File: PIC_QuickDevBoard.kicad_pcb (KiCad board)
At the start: 2 copper layers, 61.7 x 63.5 mm, 33 parts, among them J1 PICKitConnector, J10 Conn_01x08_Pin, J2 PowerSource, J3 USB_B_Micro, J4 Conn_01x08_Pin, J9 Conn_01x08_Pin, SW1 SW_Push, U1 PIC24, U2 PIC16, U3 LD1117, Y1 Crystal

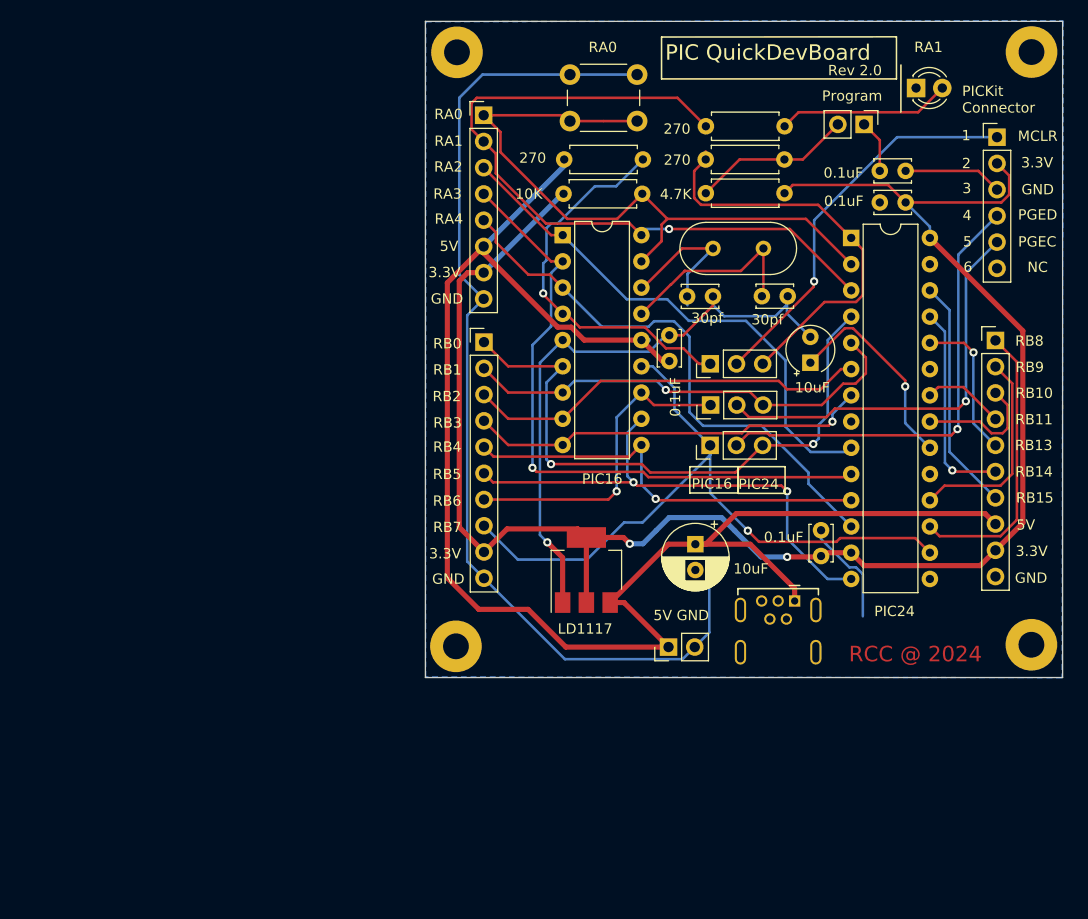
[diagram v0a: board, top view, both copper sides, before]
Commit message: fixing PICF14 vcc
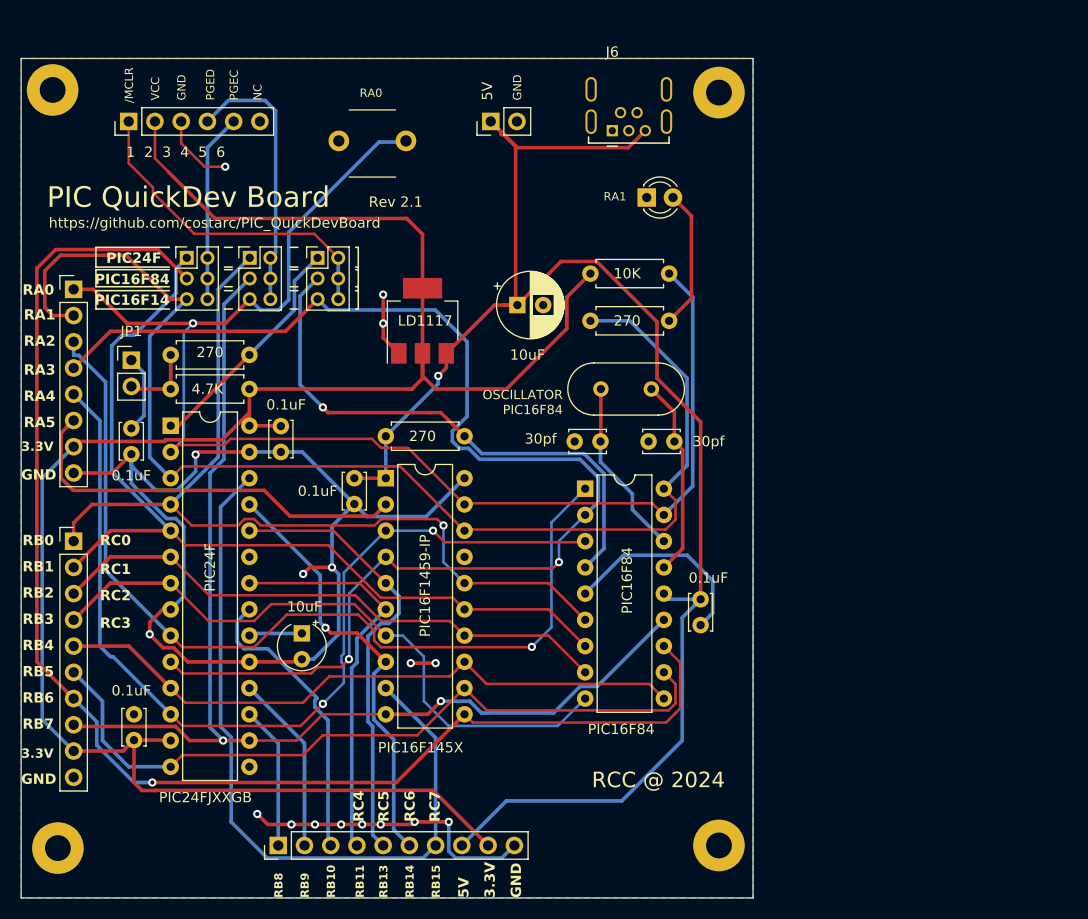
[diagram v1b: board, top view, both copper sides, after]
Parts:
- removed J10: Conn_01x08_Pin, Connector_PinHeader_2.54mm:PinHeader_1x10_P2.54mm_Vertical
- removed JP2: Jumper_MCLR, Connector_PinHeader_2.54mm:PinHeader_1x03_P2.54mm_Vertical
- removed JP3: Jumper_PGEC, Connector_PinHeader_2.54mm:PinHeader_1x03_P2.54mm_Vertical
- removed JP5: Program, Connector_PinHeader_2.54mm:PinHeader_1x02_P2.54mm_Vertical
- added C9: 0.1uF, Capacitor_THT:C_Disc_D3.4mm_W2.1mm_P2.50mm, F.Cu at (128.8, 85.4)
- added J5: PICKitConnector, Connector_PinHeader_2.54mm:PinHeader_1x06_P2.54mm_Vertical, F.Cu at (73.4, 39.1)
- added J6: USB_B_Micro, Roni_Footprints:USB_Mini-B_Tensility_4Holes, F.Cu at (120.2, 40.0)
- added J7: PGEC_LINES, Connector_PinHeader_2.00mm:PinHeader_2x03_P2.00mm_Vertical, F.Cu at (79.0, 52.3)
- added J8: PGED_LINES, Connector_PinHeader_2.00mm:PinHeader_2x03_P2.00mm_Vertical, F.Cu at (85.1, 52.3)
- added U4: PIC16F1459-IP, Package_DIP:DIP-20_W7.62mm, F.Cu at (98.3, 73.7)
- C4: value 0.1uF -> 10uF; footprint Capacitor_THT:C_Disc_D3.4mm_W2.1mm_P2.50mm -> Capacitor_THT:CP_Radial_Tantal_D4.5mm_P2.50mm
- C7: footprint Capacitor_THT:CP_Radial_Tantal_D4.5mm_P2.50mm -> Capacitor_THT:CP_Radial_D6.3mm_P2.50mm
- C8: value 10uF -> 0.1uF; footprint Capacitor_THT:CP_Radial_D6.3mm_P2.50mm -> Capacitor_THT:C_Disc_D3.4mm_W2.1mm_P2.50mm
- J1: value PICKitConnector -> Conn_01x08_Pin; footprint Connector_PinHeader_2.54mm:PinHeader_1x06_P2.54mm_Vertical -> Connector_PinHeader_2.54mm:PinHeader_1x08_P2.54mm_Vertical
- J2: value PowerSource -> Conn_01x08_Pin; footprint Connector_PinHeader_2.54mm:PinHeader_1x02_P2.54mm_Vertical -> Connector_PinHeader_2.54mm:PinHeader_1x10_P2.54mm_Vertical
- J3: value USB_B_Micro -> Conn_01x08_Pin; footprint Roni Footprints:USB_Mini-B_Tensility_4Holes -> Connector_PinHeader_2.54mm:PinHeader_1x10_P2.54mm_Vertical
- J4: value Conn_01x08_Pin -> PowerSource; footprint Connector_PinHeader_2.54mm:PinHeader_1x08_P2.54mm_Vertical -> Connector_PinHeader_2.54mm:PinHeader_1x02_P2.54mm_Vertical
- J9: value Conn_01x08_Pin -> MCLR_LINES; footprint Connector_PinHeader_2.54mm:PinHeader_1x10_P2.54mm_Vertical -> Connector_PinHeader_2.00mm:PinHeader_2x03_P2.00mm_Vertical
- JP1: value Jumper_PGED -> Program; footprint Connector_PinHeader_2.54mm:PinHeader_1x03_P2.54mm_Vertical -> Connector_PinHeader_2.54mm:PinHeader_1x02_P2.54mm_Vertical
- R3: value 10K -> 270
- R5: value 270 -> 10K
- SW1: footprint Button_Switch_THT:SW_PUSH_6mm -> Roni_Footprints:SW_PUSH_6mm_2Holes
- U1: value PIC24 -> PIC24F
- U2: value PIC16 -> PIC16F84
- moved C3 91.1 mm to (73.9, 99.0), turned to 90 degrees
- moved J1 90.6 mm to (68.1, 55.4)
- moved C1 76.6 mm to (73.7, 68.8), turned to -90 degrees
- moved U1 68.4 mm to (77.5, 68.6)
- moved J2 58.5 mm to (68.1, 79.8), turned to 0 degrees
- moved JP1 56.6 mm to (73.7, 62.2), turned to 0 degrees
- moved J3 55.3 mm to (87.9, 109.2), turned to 90 degrees
- moved R1 55.2 mm to (77.5, 65.0)
- moved C2 53.8 mm to (88.1, 68.6), turned to -90 degrees
- moved R2 48.1 mm to (85.1, 61.7), turned to 180 degrees
- moved C4 44.3 mm to (90.2, 88.7), turned to -90 degrees
- moved H3 43.2 mm to (66.5, 109.5)
- moved H1 39.3 mm to (66.0, 36.1)
- moved H4 36.0 mm to (130.6, 109.2)
- moved C8 33.6 mm to (95.2, 73.7)
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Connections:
- C1 pad 1: Net-(JP5-A) -> Net-(JP1-A)
- C4 pad 1: 5V -> Net-(U1-Vcap/Vddcore)
- C7 pad 1: Net-(U1-Vcap/Vddcore) -> 5V
- J1 pad 1: /MCLR -> PIC16F14_PGED
- J1 pad 2: 3.3V -> PIC16F14_PGEC
- J1 pad 3: GND -> RA2
- J1 pad 4: PGED -> PIC16F14_MCLR
- J1 pad 5: PGEC -> RA4
- J1 pad 6: unconnected-(J1-Pin_6-Pad6) -> RA5
- J2 pad 1: 5V -> PIC24_PGED
- J2 pad 2: GND -> PIC24_PGEC
- J3 pad 1: 5V -> RB8
- J3 pad 2: unconnected-(J3-D--Pad2) -> RB9
- J3 pad 3: unconnected-(J3-D+-Pad3) -> RB10
- J3 pad 4: unconnected-(J3-ID-Pad4) -> RB11
- J3 pad 5: GND -> RB13
- J3 pad 6: GND -> RB14
- J4 pad 1: RA0 -> 5V
- J4 pad 2: RA1 -> GND
- J9 pad 1: PIC24_PGED -> PIC24_MCLR
- J9 pad 2: PIC24_PGEC -> /MCLR
- J9 pad 3: RB2 -> PIC16F84_MCLR
- J9 pad 4: RB3 -> /MCLR
- J9 pad 5: RB4 -> PIC16F14_MCLR
- J9 pad 6: RB5 -> /MCLR
- JP1 pad 1: PIC16_PGED -> Net-(JP1-A)
- JP1 pad 2: PGED -> Net-(JP1-B)
- R1 pad 1: Net-(JP5-B) -> Net-(JP1-B)
- R2 pad 2: Net-(JP5-B) -> Net-(JP1-B)
- R3 pad 1: 3.3V -> PIC16F84_MCLR
- R3 pad 2: RA0 -> 5V
- R4 pad 1: RA1 -> PIC16F14_PGEC
- R5 pad 1: PIC16_MCLR -> 3.3V
- R5 pad 2: 5V -> PIC16F14_PGED
- SW1 pad 2: RA0 -> PIC16F14_PGED
- U1 pad 10: RA3 -> PIC16F14_MCLR
- U1 pad 16: PIC16_PGED -> PIC16F84_PGED
- U1 pad 2: RA0 -> PIC16F14_PGED
- U1 pad 3: RA1 -> PIC16F14_PGEC
- U2 pad 12: PIC16_PGEC -> PIC16F84_PGEC
- U2 pad 13: PIC16_PGED -> PIC16F84_PGED
- U2 pad 17: RA0 -> PIC16F14_PGED
- U2 pad 18: RA1 -> PIC16F14_PGEC
- U2 pad 2: RA3 -> PIC16F14_MCLR
- U2 pad 4: PIC16_MCLR -> PIC16F84_MCLR
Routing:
- net PIC16F14_PGED: track 0.00 -> 135.8 mm, vias 0 -> 1
- net PIC16F84_PGEC: track 0.00 -> 133.3 mm, vias 0 -> 1
- net PIC16F14_MCLR: track 0.00 -> 125.3 mm, vias 0 -> 2
- net PIC16F14_PGEC: track 0.00 -> 121.6 mm
- net PIC16F84_PGED: track 0.00 -> 110.4 mm, vias 0 -> 2
- net RA1: track 71.7 -> 0.00 mm, vias 1 -> 0
- net PIC16_PGED: track 68.0 -> 0.00 mm, vias 1 -> 0
- net RA0: track 65.0 -> 0.00 mm
- net RA3: track 63.0 -> 0.00 mm, vias 1 -> 0
- net PIC16F84_MCLR: track 0.00 -> 53.8 mm, vias 0 -> 1
- net RB15: track 22.7 -> 73.9 mm
- net PIC24_PGEC: track 44.2 -> 88.1 mm, vias 1 -> 0
- net RA5: track 0.00 -> 39.5 mm
- net PIC16_MCLR: track 38.0 -> 0.00 mm, vias 1 -> 0
- net RA2: track 50.9 -> 88.8 mm, vias 0 -> 1
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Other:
- board size 61.7 x 63.5 mm -> 70.9 x 81.3 mm
- board text added: "/MCLR"
- board text added: "1 2 3 4 5 6"
- board text added: "OSCILLATOR PIC16F84"
- board text added: "PIC QuickDev Board"
- board text added: "PIC16F14"
- board text added: "PIC16F145X"
- board text added: "PIC16F84"
- board text added: "PIC24F"
- board text added: "PIC24FJXXGB"
- board text added: "RA5"
- board text added: "RC0"
- board text added: "RC1"
- board text added: "RC2"
- board text added: "RC3"
- board text added: "RC4"
- board text added: "RC5"
- board text added: "RC6"
- board text added: "RC7"
- board text added: "Rev 2.1"
- board text added: "VCC"
- board text removed: "1"
- board text removed: "2"
- board text removed: "3"
- board text removed: "4"
- board text removed: "5"
- board text removed: "5V GND"
- board text removed: "6"
- board text removed: "For PIC16 use: Insert the 3 jumpers in position {dblquote}PIC16{dblquote} For PIC24 use: Insert the 3 jumpers in position {dblquote}PIC24{dblquote}"
- board text removed: "Jumper {dblquote}Program{dblquote}: Remove to program the PIC24"
- board text removed: "MCLR"
- board text removed: "PIC QuickDevBoard"
- board text removed: "PIC16"
- board text removed: "PIC24"
- board text removed: "PICKit Connector"
- board text removed: "Rev 2.0"

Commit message: Updated PCB to REv 2.1 with fix to VCC for PIC16F
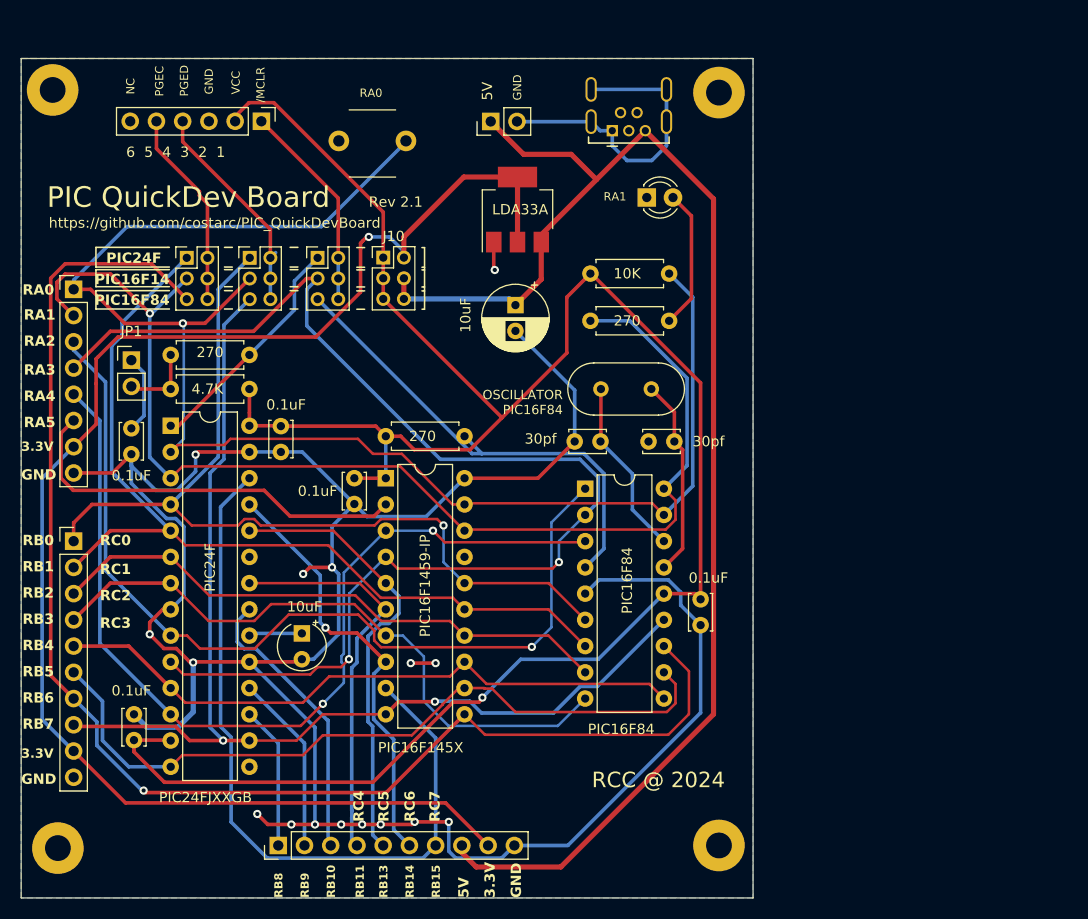
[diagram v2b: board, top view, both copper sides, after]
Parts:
- added J10: VCC Lines, Connector_PinHeader_2.00mm:PinHeader_2x03_P2.00mm_Vertical, F.Cu at (98.0, 52.3)
- U3: value LD1117 -> LDA33A
- moved U3 14.2 mm to (111.0, 47.6)
- moved J5 12.8 mm to (86.2, 39.1), turned to -90 degrees
- moved C7 0.19 mm to (110.8, 56.9), turned to -90 degrees
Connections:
- C2 pad 1: 3.3V -> VCC
- C3 pad 1: 3.3V -> VCC
- C7 pad 1: 5V -> +5V
- C8 pad 1: 5V -> VCC
- C9 pad 1: 5V -> VCC
- J1 pad 7: 3.3V -> +3.3V
- J2 pad 9: 3.3V -> +3.3V
- J3 pad 8: 5V -> +5V
- J3 pad 9: 3.3V -> +3.3V
- J4 pad 1: 5V -> +5V
- J5 pad 2: 3.3V -> VCC
- J6 pad 1: 5V -> +5V
- J7 pad 3: PIC16F84_PGEC -> PIC16F14_PGEC
- J7 pad 5: PIC16F14_PGEC -> PIC16F84_PGEC
- J8 pad 3: PIC16F84_PGED -> PIC16F14_PGED
- J8 pad 5: PIC16F14_PGED -> PIC16F84_PGED
- J9 pad 3: PIC16F84_MCLR -> PIC16F14_MCLR
- J9 pad 5: PIC16F14_MCLR -> PIC16F84_MCLR
- R1 pad 2: 3.3V -> VCC
- R3 pad 2: 5V -> VCC
- R5 pad 1: 3.3V -> VCC
- U1 pad 13: 3.3V -> VCC
- U1 pad 28: 3.3V -> VCC
- U2 pad 14: 5V -> VCC
- U3 pad 2: 3.3V -> +3.3V
- U3 pad 3: 5V -> +5V
- U4 pad 1: 5V -> VCC
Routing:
- net VCC: track 0.00 -> 204.5 mm, vias 0 -> 1
- net 3.3V: track 196.8 -> 0.00 mm
- net 5V: track 153.2 -> 0.00 mm, vias 1 -> 0
- net +3.3V: track 0.00 -> 146.4 mm, vias 0 -> 1
- net +5V: track 0.00 -> 139.1 mm
- net GND: track 171.6 -> 272.6 mm, vias 17 -> 16
- net PIC16F14_PGED: track 135.8 -> 148.8 mm
- net /MCLR: track 32.4 -> 20.3 mm
- net PIC16F84_MCLR: track 53.8 -> 46.9 mm, vias 1 -> 0
- net PIC16F14_PGEC: track 121.6 -> 115.7 mm, vias 0 -> 1
- net PGED: track 26.3 -> 21.5 mm
- net PIC16F84_PGED: track 110.4 -> 108.4 mm
- net PIC16F14_MCLR: track 125.3 -> 123.6 mm
- net PGEC: track 18.3 -> 19.3 mm
- net RB10: track 28.6 -> 27.8 mm
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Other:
- board text added: "6 5 4 3 2 1"
- board text removed: "1 2 3 4 5 6"

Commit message: Revision 2.2
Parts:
- moved R3 14.6 mm to (112.8, 82.5), turned to 90 degrees
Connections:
- J1 pad 1: PIC16F14_PGED -> RA0
- J1 pad 2: PIC16F14_PGEC -> RA1
- J2 pad 1: PIC24_PGED -> PIC16F14_PGED
- J2 pad 2: PIC24_PGEC -> PIC16F14_PGEC
- J7 pad 1: PIC24_PGEC -> PIC16F14_PGEC
- J8 pad 1: PIC24_PGED -> PIC16F14_PGED
- R4 pad 1: PIC16F14_PGEC -> RA1
- R5 pad 2: PIC16F14_PGED -> RA0
- SW1 pad 2: PIC16F14_PGED -> RA0
- U1 pad 2: PIC16F14_PGED -> RA0
- U1 pad 3: PIC16F14_PGEC -> RA1
- U1 pad 4: PIC24_PGED -> PIC16F14_PGED
- U1 pad 5: PIC24_PGEC -> PIC16F14_PGEC
- U2 pad 17: PIC16F14_PGED -> RA0
- U2 pad 18: PIC16F14_PGEC -> RA1
- U2 pad 6: PIC24_PGED -> PIC16F14_PGED
- U2 pad 7: PIC24_PGEC -> PIC16F14_PGEC
- U4 pad 15: PIC24_PGEC -> PIC16F14_PGEC
- U4 pad 16: PIC24_PGED -> PIC16F14_PGED
- U4 pad 18: PIC16F14_PGEC -> RA1
- U4 pad 19: PIC16F14_PGED -> RA0
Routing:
- net RA0: track 0.00 -> 147.7 mm
- net RA1: track 0.00 -> 98.8 mm, vias 0 -> 1
- net PIC24_PGEC: track 87.4 -> 0.00 mm
- net PIC24_PGED: track 86.8 -> 0.00 mm, vias 1 -> 0
- net PIC16F14_PGED: track 148.8 -> 86.8 mm
- net PIC16F14_PGEC: track 115.7 -> 87.9 mm, vias 1 -> 0
- net VCC: track 204.5 -> 226.1 mm
- net PIC16F84_MCLR: track 46.9 -> 49.5 mm
- net PIC16F84_PGEC: track 133.9 -> 134.8 mm
- net PIC16F14_MCLR: track 123.6 -> 122.9 mm
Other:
- board text added: "Rev 2.2"
- board text removed: "Rev 2.1"

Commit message: Progressing with calibration code
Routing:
- net GND: track 272.8 -> 242.6 mm
- net +5V: track 139.1 -> 136.7 mm
